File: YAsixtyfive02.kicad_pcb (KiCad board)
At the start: 2 copper layers, 99.7 x 99.7 mm, 59 parts, among them J1 ~{NMI}, J2 Aux 5VDC, J3 Power 5V, J4 Expansion Bus, J7 GND, J8 FTDI Serial2USB, SW1 RESET, SW2 SW_Push_DPDT, U1 WD65C02, U10 74LS138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

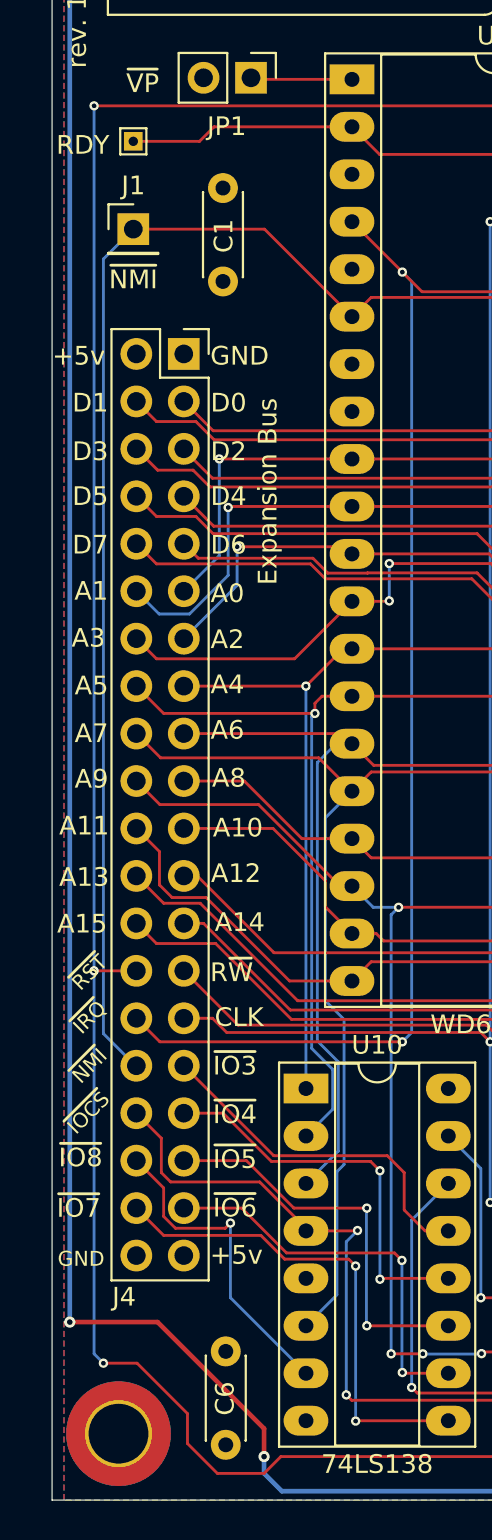
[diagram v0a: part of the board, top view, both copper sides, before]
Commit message: monor routing revision clean DRC
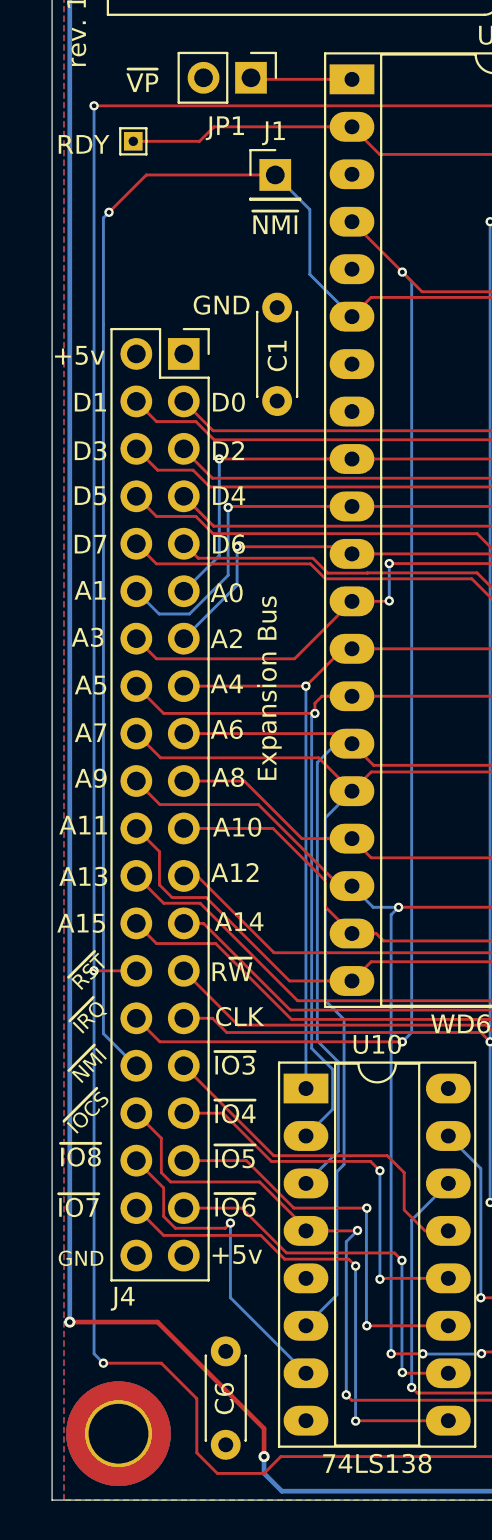
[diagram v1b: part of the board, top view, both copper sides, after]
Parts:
- moved J1 8.13 mm to (43.1, 78.9)
- moved C1 7.03 mm to (43.2, 91.0)
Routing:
- net ~{NMI}: track 88.5 -> 94.3 mm, vias 0 -> 1
- net ~{RESET}: track 238.9 -> 239.7 mm
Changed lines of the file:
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@@
       (effects (font (size 1 1) (thickness 0.15)))
     )
-    (fp_text value "Expansion Bus" (at 4.4958 7.366 90) (layer "F.SilkS")
+    (fp_text value "Expansion Bus" (at 4.4958 17.92 90) (layer "F.SilkS")
       (effects (font (size 1 1) (thickness 0.15)))
     )
@@
     (property "Sheetname" "")
     (attr through_hole)
-    (fp_text reference "JP1" (at 2.6 1.3 180) (layer "F.SilkS")
+    (fp_text reference "JP1" (at 2.6 1.3) (layer "F.SilkS")
       (effects (font (size 1 1) (thickness 0.15)))
     )
-    (fp_text value "~{VP}" (at 0.3 5.8 180) (layer "F.SilkS")
+    (fp_text value "~{VP}" (at 0.3 5.8) (layer "F.SilkS")
       (effects (font (size 1 1) (thickness 0.15)))
     )
@@
   )
   (footprint "Capacitor_THT:C_Disc_D4.3mm_W1.9mm_P5.00mm" (layer "F.Cu")
-    (at 40.2616 84.6292 90)
+    (at 43.1616 91.0292 90)
     (descr "C, Disc series, Radial, pin pitch=5.00mm, , diameter*width=4.3*1.9mm^2, Capacitor, http://www.vishay.com/docs/45233/krseries.pdf")
     (tags "C Disc series Radial pin pitch 5.00mm  diameter 4.3mm width 1.9mm Capacitor")
@@
   )
   (footprint "Connector_PinHeader_2.54mm:PinHeader_1x01_P2.54mm_Vertical" (layer "F.Cu")
-    (at 35.4616 81.8292)
+    (at 43.0616 78.9292)
     (descr "Through hole straight pin header, 1x01, 2.54mm pitch, single row")
     (tags "Through hole pin header THT 1x01 2.54mm single row")
@@
     (effects (font (size 0.8 0.8) (thickness 0.15)))
   )
-  (gr_text "GND" (at 42.7244 88.616) (layer "F.SilkS")
+  (gr_text "GND" (at 41.7616 85.9292) (layer "F.SilkS")
     (effects (font (size 1 1) (thickness 0.15)) (justify right))
   )
@@
   (segment (start 60.8664 121.0439) (end 60.8664 122.634) (width 0.1524) (layer "B.Cu") (net 26))
   (segment (start 96.6616 121.2292) (end 98.0616 119.8292) (width 0.1524) (layer "B.Cu") (net 26))
-  (segment (start 39.9616 148.4292) (end 38.3616 146.8292) (width 0.1524) (layer "F.Cu") (net 27))
-  (segment (start 43.3616 147.5292) (end 42.4616 148.4292) (width 0.1524) (layer "F.Cu") (net 27))
+  (segment (start 38.8616 147.3292) (end 38.8616 144.4292) (width 0.1524) (layer "F.Cu") (net 27))
+  (segment (start 82.5616 146.8292) (end 81.8616 147.5292) (width 0.1524) (layer "F.Cu") (net 27))
   (segment (start 33.3616 75.2292) (end 60.991 75.2292) (width 0.1524) (layer "F.Cu") (net 27))
-  (segment (start 38.3616 146.8292) (end 38.3616 145.2292) (width 0.1524) (layer "F.Cu") (net 27))
+  (segment (start 36.9616 142.5292) (end 33.8616 142.5292) (width 0.1524) (layer "F.Cu") (net 27))
   (segment (start 33.3616 121.5292) (end 35.6244 121.5292) (width 0.1524) (layer "F.Cu") (net 27))
   (segment (start 82.9116 74.4292) (end 116.6991 74.4292) (width 0.1524) (layer "F.Cu") (net 27))
-  (segment (start 42.4616 148.4292) (end 39.9616 148.4292) (width 0.1524) (layer "F.Cu") (net 27))
+  (segment (start 39.9616 148.4292) (end 38.8616 147.3292) (width 0.1524) (layer "F.Cu") (net 27))
   (segment (start 60.991 75.2292) (end 62.4078 73.8124) (width 0.1524) (layer "F.Cu") (net 27))
+  (segment (start 81.8616 147.5292) (end 43.3616 147.5292) (width 0.1524) (layer "F.Cu") (net 27))
+  (segment (start 38.8616 144.4292) (end 36.9616 142.5292) (width 0.1524) (layer "F.Cu") (net 27))
   (segment (start 94.9616 144.7292) (end 91.1616 144.7292) (width 0.1524) (layer "F.Cu") (net 27))
   (segment (start 91.1616 144.7292) (end 89.0616 146.8292) (width 0.1524) (layer "F.Cu") (net 27))
-  (segment (start 82.5616 146.8292) (end 81.8616 147.5292) (width 0.1524) (layer "F.Cu") (net 27))
   (segment (start 116.6991 74.4292) (end 116.7616 74.3667) (width 0.1524) (layer "F.Cu") (net 27))
-  (segment (start 38.3616 145.2292) (end 35.6616 142.5292) (width 0.1524) (layer "F.Cu") (net 27))
+  (segment (start 42.4616 148.4292) (end 39.9616 148.4292) (width 0.1524) (layer "F.Cu") (net 27))
   (segment (start 82.0616 75.2792) (end 82.9116 74.4292) (width 0.1524) (layer "F.Cu") (net 27))
   (segment (start 89.0616 146.8292) (end 82.5616 146.8292) (width 0.1524) (layer "F.Cu") (net 27))
-  (segment (start 81.8616 147.5292) (end 43.3616 147.5292) (width 0.1524) (layer "F.Cu") (net 27))
-  (segment (start 35.6616 142.5292) (end 33.8616 142.5292) (width 0.1524) (layer "F.Cu") (net 27))
+  (segment (start 43.3616 147.5292) (end 42.4616 148.4292) (width 0.1524) (layer "F.Cu") (net 27))
   (segment (start 62.4078 73.8124) (end 67.564 73.8124) (width 0.1524) (layer "F.Cu") (net 27))
   (segment (start 67.564 73.8124) (end 67.6656 73.7108) (width 0.1524) (layer "F.Cu") (net 27))
@@
   (segment (start 90.01206 58.54) (end 89.7616 58.54) (width 0.1524) (layer "B.Cu") (net 49))
   (segment (start 97.7616 70.4292) (end 95.1616 67.8292) (width 0.1524) (layer "B.Cu") (net 49))
+  (segment (start 34.1616 80.9292) (end 36.1616 78.9292) (width 0.1524) (layer "F.Cu") (net 50))
   (segment (start 67.1702 85.4838) (end 68.5156 86.8292) (width 0.1524) (layer "F.Cu") (net 50))
   (segment (start 68.5156 89.2432) (end 69.4016 90.1292) (width 0.1524) (layer "F.Cu") (net 50))
-  (segment (start 47.1678 86.5124) (end 42.4846 81.8292) (width 0.1524) (layer "F.Cu") (net 50))
   (segment (start 48.1964 85.4838) (end 67.1702 85.4838) (width 0.1524) (layer "F.Cu") (net 50))
   (segment (start 69.4016 90.1292) (end 72.1016 90.1292) (width 0.1524) (layer "F.Cu") (net 50))
-  (segment (start 42.4846 81.8292) (end 35.4616 81.8292) (width 0.1524) (layer "F.Cu") (net 50))
+  (segment (start 36.1616 78.9292) (end 43.0616 78.9292) (width 0.1524) (layer "F.Cu") (net 50))
   (segment (start 47.1678 86.5124) (end 48.1964 85.4838) (width 0.1524) (layer "F.Cu") (net 50))
   (segment (start 68.5156 86.8292) (end 68.5156 89.2432) (width 0.1524) (layer "F.Cu") (net 50))
-  (segment (start 33.8616 83.4292) (end 35.4616 81.8292) (width 0.1524) (layer "B.Cu") (net 50))
-  (segment (start 35.583 126.6092) (end 33.8616 124.8878) (width 0.1524) (layer "B.Cu") (net 50))
-  (segment (start 35.6244 126.6092) (end 35.583 126.6092) (width 0.1524) (layer "B.Cu") (net 50))
-  (segment (start 33.8616 124.8878) (end 33.8616 83.4292) (width 0.1524) (layer "B.Cu") (net 50))
+  (via (at 34.1616 80.9292) (size 0.5) (drill 0.25) (layers "F.Cu" "B.Cu") (net 50))
+  (segment (start 44.9116 80.7792) (end 44.9116 84.2562) (width 0.1524) (layer "B.Cu") (net 50))
+  (segment (start 33.8616 124.8878) (end 35.583 126.6092) (width 0.1524) (layer "B.Cu") (net 50))
+  (segment (start 33.8616 86.9292) (end 33.8616 81.2292) (width 0.1524) (layer "B.Cu") (net 50))
+  (segment (start 33.8616 81.2292) (end 34.1616 80.9292) (width 0.1524) (layer "B.Cu") (net 50))
+  (segment (start 44.9116 84.2562) (end 47.1678 86.5124) (width 0.1524) (layer "B.Cu") (net 50))
+  (segment (start 43.0616 78.9292) (end 44.9116 80.7792) (width 0.1524) (layer "B.Cu") (net 50))
+  (segment (start 35.583 126.6092) (end 35.6244 126.6092) (width 0.1524) (layer "B.Cu") (net 50))
+  (segment (start 33.8616 86.9292) (end 33.8616 124.8878) (width 0.1524) (layer "B.Cu") (net 50))
   (segment (start 126.7116 71.5792) (end 128.2316 71.5792) (width 0.1524) (layer "F.Cu") (net 52))
   (segment (start 125.3616 63.4292) (end 125.3616 70.2292) (width 0.1524) (layer "F.Cu") (net 52))

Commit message: rev 1.6.1 ready. minor routing updates and acia CS fixed
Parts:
- C8: footprint Capacitor_THT:CP_Radial_D8.0mm_P3.80mm -> Capacitor_THT:CP_Radial_D6.3mm_P2.50mm
- JP3: value Power SEL -> POWER SEL
- TP1, TP2, TP7: footprint TestPoint:TestPoint_THTPad_2.0x2.0mm_Drill1.0mm -> TestPoint:TestPoint_THTPad_1.5x1.5mm_Drill0.7mm
- TP3: value ACIA IRQ -> ACIA_IRQ
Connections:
- U10 pad 5: +5V -> GND
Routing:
- net ~{RESET}: track 239.7 -> 241.9 mm
- net USB_5V: track 220.7 -> 222.5 mm
- net ~{NMI}: track 94.3 -> 95.8 mm
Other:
- board text added: "rev. 1.6.1"
- board text removed: "ACIA $8010 - $801F"
- board text removed: "rev. 1.6.0"

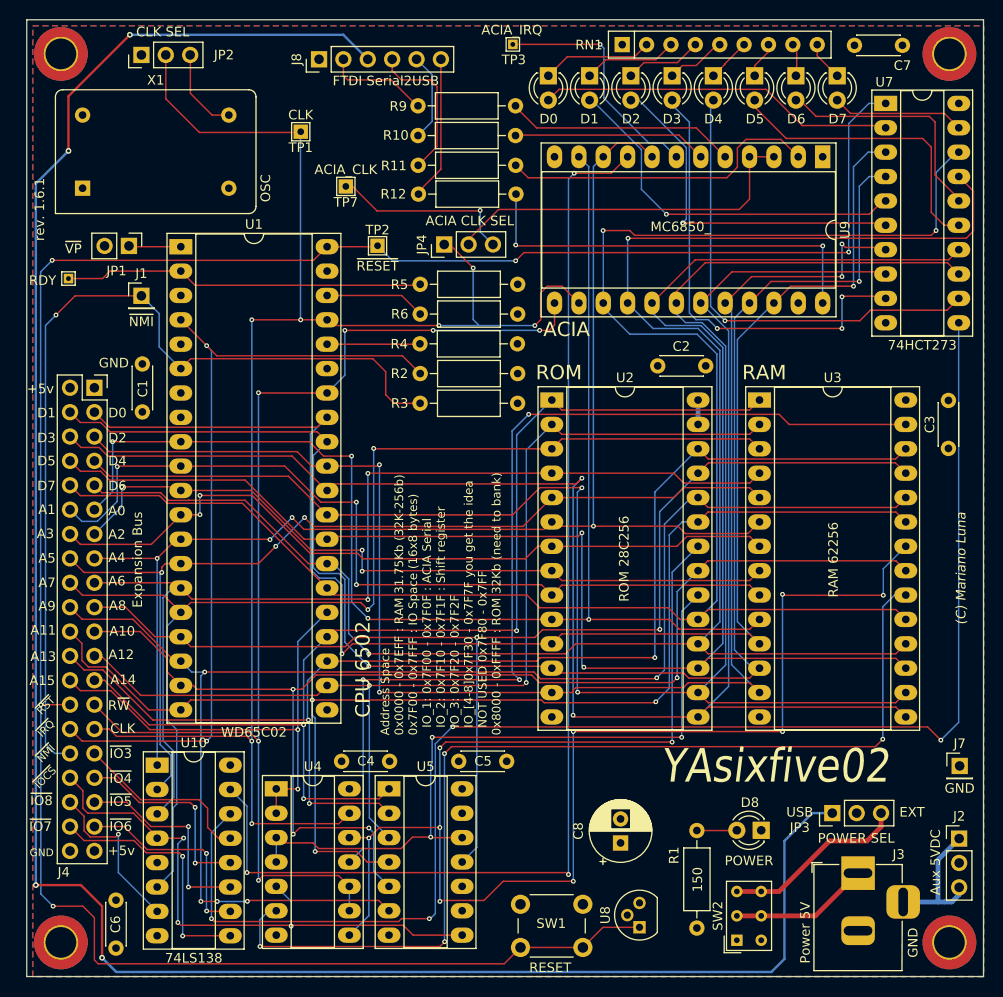
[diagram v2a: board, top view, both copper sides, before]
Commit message: Schematic and PCB Updated
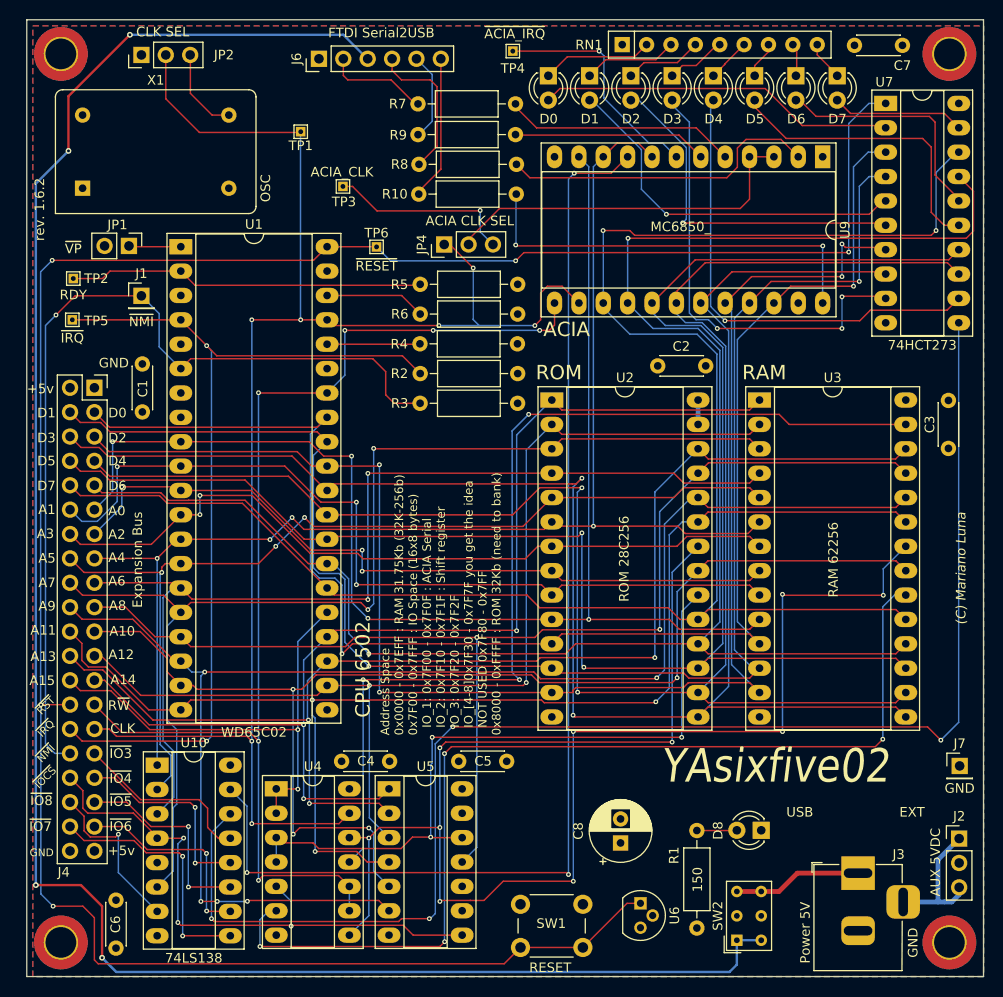
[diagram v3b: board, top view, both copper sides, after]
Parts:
- removed J8: FTDI Serial2USB, Connector_PinHeader_2.54mm:PinHeader_1x06_P2.54mm_Vertical
- removed JP3: POWER SEL, Connector_PinHeader_2.54mm:PinHeader_1x03_P2.54mm_Vertical
- removed R11, R12: 2K7, Resistor_THT:R_Axial_DIN0207_L6.3mm_D2.5mm_P10.16mm_Horizontal
- removed TP7: ACIA_CLK, TestPoint:TestPoint_THTPad_1.5x1.5mm_Drill0.7mm
- removed U8: DS1813, Package_TO_SOT_THT:TO-92
- added J6: FTDI Serial2USB, Connector_PinHeader_2.54mm:PinHeader_1x06_P2.54mm_Vertical, F.Cu at (61.6, 54.2)
- added R7: 2K7, Resistor_THT:R_Axial_DIN0207_L6.3mm_D2.5mm_P10.16mm_Horizontal, F.Cu at (71.9, 58.9)
- added R8: 2K7, Resistor_THT:R_Axial_DIN0207_L6.3mm_D2.5mm_P10.16mm_Horizontal, F.Cu at (82.1, 65.2)
- added TP5: ~{IRQ}, TestPoint:TestPoint_THTPad_1.0x1.0mm_Drill0.5mm, F.Cu at (35.9, 81.4)
- added TP6: ~{RESET}, TestPoint:TestPoint_THTPad_1.0x1.0mm_Drill0.5mm, F.Cu at (67.6, 73.8)
- added U6: DS1813, Package_TO_SOT_THT:TO-92, F.Cu at (95.1, 142.2)
- D0, D1, D2, D3, D4, D5, D6, D7, D8: footprint LED_THT:LED_D3.0mm -> LED_THT:LED_SMALL_3.0mm
- J2: value Aux 5VDC -> AUX 5VDC
- SW2: value SW_Push_DPDT -> Power SW
- TP1: footprint TestPoint:TestPoint_THTPad_1.5x1.5mm_Drill0.7mm -> TestPoint:TestPoint_THTPad_1.0x1.0mm_Drill0.5mm
- TP2: value ~{RESET} -> RDY; footprint TestPoint:TestPoint_THTPad_1.5x1.5mm_Drill0.7mm -> TestPoint:TestPoint_THTPad_1.0x1.0mm_Drill0.5mm
- TP3: value ACIA_IRQ -> ACIA_CLK
- TP4: value RDY -> ~{ACIA_IRQ}
- moved TP4 52.0 mm to (81.8, 53.4)
- moved TP2 31.9 mm to (36.0, 77.1)
- moved TP3 23.1 mm to (64.1, 67.5)
- moved R10 11.8 mm to (72.0, 68.3), turned to 0 degrees
- moved R9 3.00 mm to (82.0, 62.1)
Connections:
- net /Aux_0v renamed /Power and Aux/Aux_GND
- net /OSC_OUT renamed /Power and Aux/OSC_OUT
- net /TX_CLK renamed TX_CLK
- R10 pad 1: TxD -> /Power and Aux/RTS
- R10 pad 2: /RX -> ~{CTS}
- R9 pad 1: ~{RTS} -> TxD
- R9 pad 2: /CTS -> /Power and Aux/RX
- SW2 pad 1: unconnected-(SW2-Pad1) -> USB_5V
- SW2 pad 2: EXT_5V -> +5V
- SW2 pad 3: SW_5V -> EXT_5V
- SW2 pad 4: unconnected-(SW2-Pad4) -> USB_5V
- SW2 pad 5: EXT_5V -> +5V
- SW2 pad 6: SW_5V -> EXT_5V
- TP2 pad 1: ~{RESET} -> RDY
- TP3 pad 1: ~{ACIA_IRQ} -> ACIA_CLK
- TP4 pad 1: RDY -> ~{ACIA_IRQ}
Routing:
- net SW_5V: track 19.2 -> 0.00 mm
- net USB_5V: track 222.5 -> 203.8 mm
- net /TX: track 15.6 -> 0.00 mm
- net /Power and Aux/TX: track 0.00 -> 15.5 mm
- net /Power and Aux/RTS: track 0.00 -> 15.1 mm
- net /RTS: track 15.0 -> 0.00 mm
- net ~{IRQ}: track 83.6 -> 94.9 mm
- net /CTS: track 10.8 -> 0.00 mm
- net /Power and Aux/CTS: track 0.00 -> 10.7 mm
- net /Power and Aux/RX: track 0.00 -> 9.29 mm
- net /RX: track 9.24 -> 0.00 mm
- net EXT_5V: track 14.5 -> 13.4 mm
- net ~{RESET}: track 241.9 -> 242.9 mm
- net ~{ACIA_IRQ}: track 24.9 -> 24.2 mm
- net RDY: track 37.6 -> 37.1 mm
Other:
- board text added: "rev. 1.6.2"
- board text removed: "rev. 1.6.1"

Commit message: 6502 Bus Edge Connector done
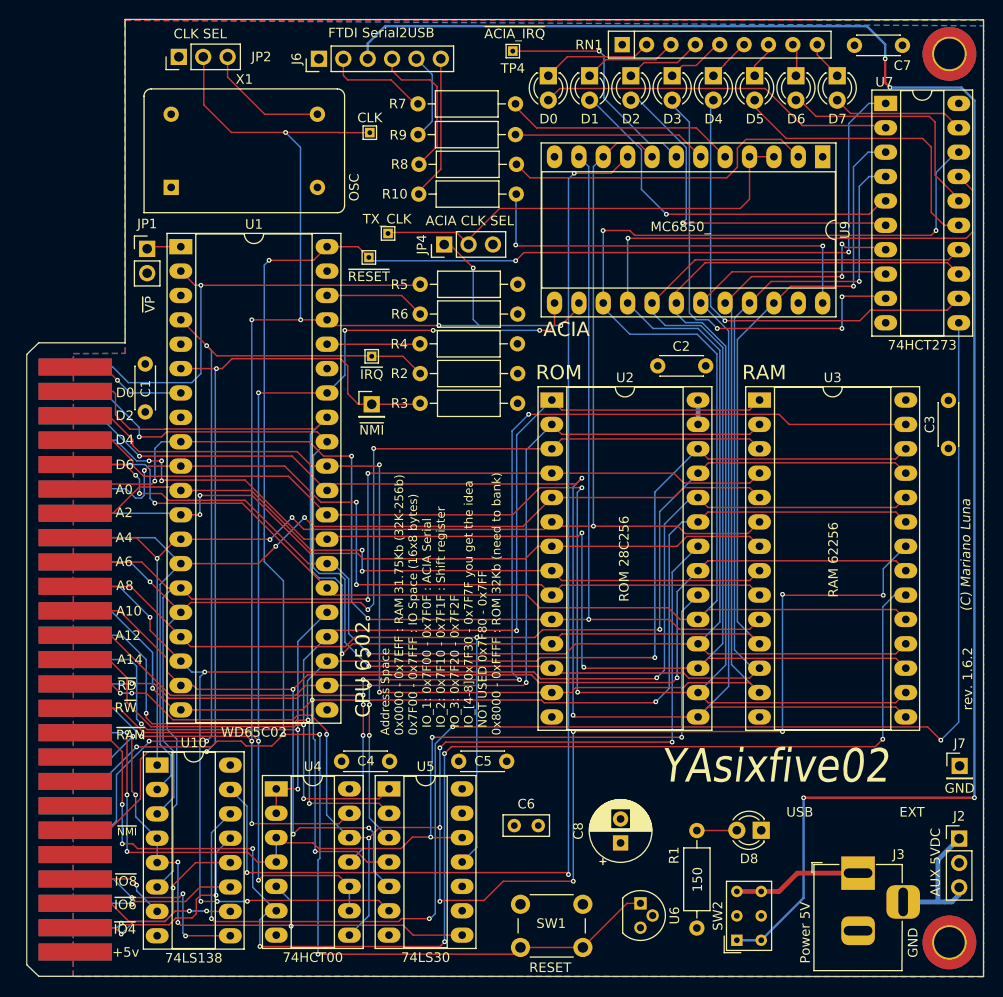
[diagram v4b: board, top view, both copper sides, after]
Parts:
- removed H3, H4: MNT, MountingHole:MountingHole_3.2mm_M3_DIN965_Pad_TopBottom
- removed J4: Expansion Bus, Connector_PinSocket_2.54mm:PinSocket_2x20_P2.54mm_Vertical
- removed TP2: RDY, TestPoint:TestPoint_THTPad_1.0x1.0mm_Drill0.5mm
- added 6502_BUS1: 6502_BUS, Apple2 Edge:BUS_A2, F.Cu at (36.2, 109.2)
- C6: footprint Capacitor_THT:C_Disc_D4.3mm_W1.9mm_P5.00mm -> Capacitor_THT:C_Rect_L4.6mm_W2.0mm_P2.50mm_MKS02_FKP02
- D8: footprint LED_THT:LED_SMALL_3.0mm -> LED_THT:LED_D3.0mm
- TP3: value ACIA_CLK -> TX_CLK
- moved C6 42.2 mm to (81.9, 134.1), turned to 0 degrees
- moved TP5 31.4 mm to (67.1, 85.2)
- moved J1 26.5 mm to (67.1, 90.2)
- moved X1 9.23 mm to (46.2, 67.6)
- moved TP1 7.20 mm to (66.9, 61.9)
- moved TP3 6.79 mm to (68.8, 72.4)
- moved JP2 3.91 mm to (47.0, 54.0)
- moved JP1 1.92 mm to (43.7, 74.0), turned to 0 degrees
- moved TP6 1.36 mm to (66.8, 74.9)
- moved C1 0.30 mm to (43.5, 91.0)
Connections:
- TP3 pad 1: ACIA_CLK -> TX_CLK
- U1 pad 7: unconnected-(U1-Pad7) -> SYNC
- U10 pad 5: GND -> ~{IO_CS}
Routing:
- net ~{RD}: track 165.9 -> 206.7 mm, vias 10 -> 13
- net ~{RAM_CS}: track 106.9 -> 143.6 mm, vias 4 -> 7
- net ~{ROM_CS}: track 74.9 -> 108.7 mm, vias 3 -> 6
- net ~{WR}: track 104.3 -> 135.1 mm, vias 3 -> 7
- net ~{RESET}: track 242.9 -> 217.2 mm, vias 5 -> 7
- net USB_5V: track 203.8 -> 180.8 mm
- net ACIA_CLK: track 19.5 -> 0.00 mm, vias 1 -> 0
- net SYNC: track 0.00 -> 12.1 mm, vias 0 -> 1
- net RDY: track 37.1 -> 49.0 mm, vias 0 -> 1
- net TX_CLK: track 38.5 -> 47.4 mm
- net ~{IO_8}: track 17.3 -> 10.3 mm
- net ~{NMI}: track 95.8 -> 88.9 mm, vias 1 -> 2
- net ~{IRQ}: track 94.9 -> 89.3 mm, vias 2 -> 3
- net ~{IO_CS}: track 59.7 -> 64.7 mm, vias 3 -> 5
- net ~{IO_7}: track 26.3 -> 21.4 mm, vias 2 -> 3
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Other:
- outline, holes or cut-outs redrawn
- board text added: "~{RAM}"
- board text added: "~{RD}"
